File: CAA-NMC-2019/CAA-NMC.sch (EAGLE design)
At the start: 41 parts, among them IC1 ATTINY85-20SU, J1 M20-9980346

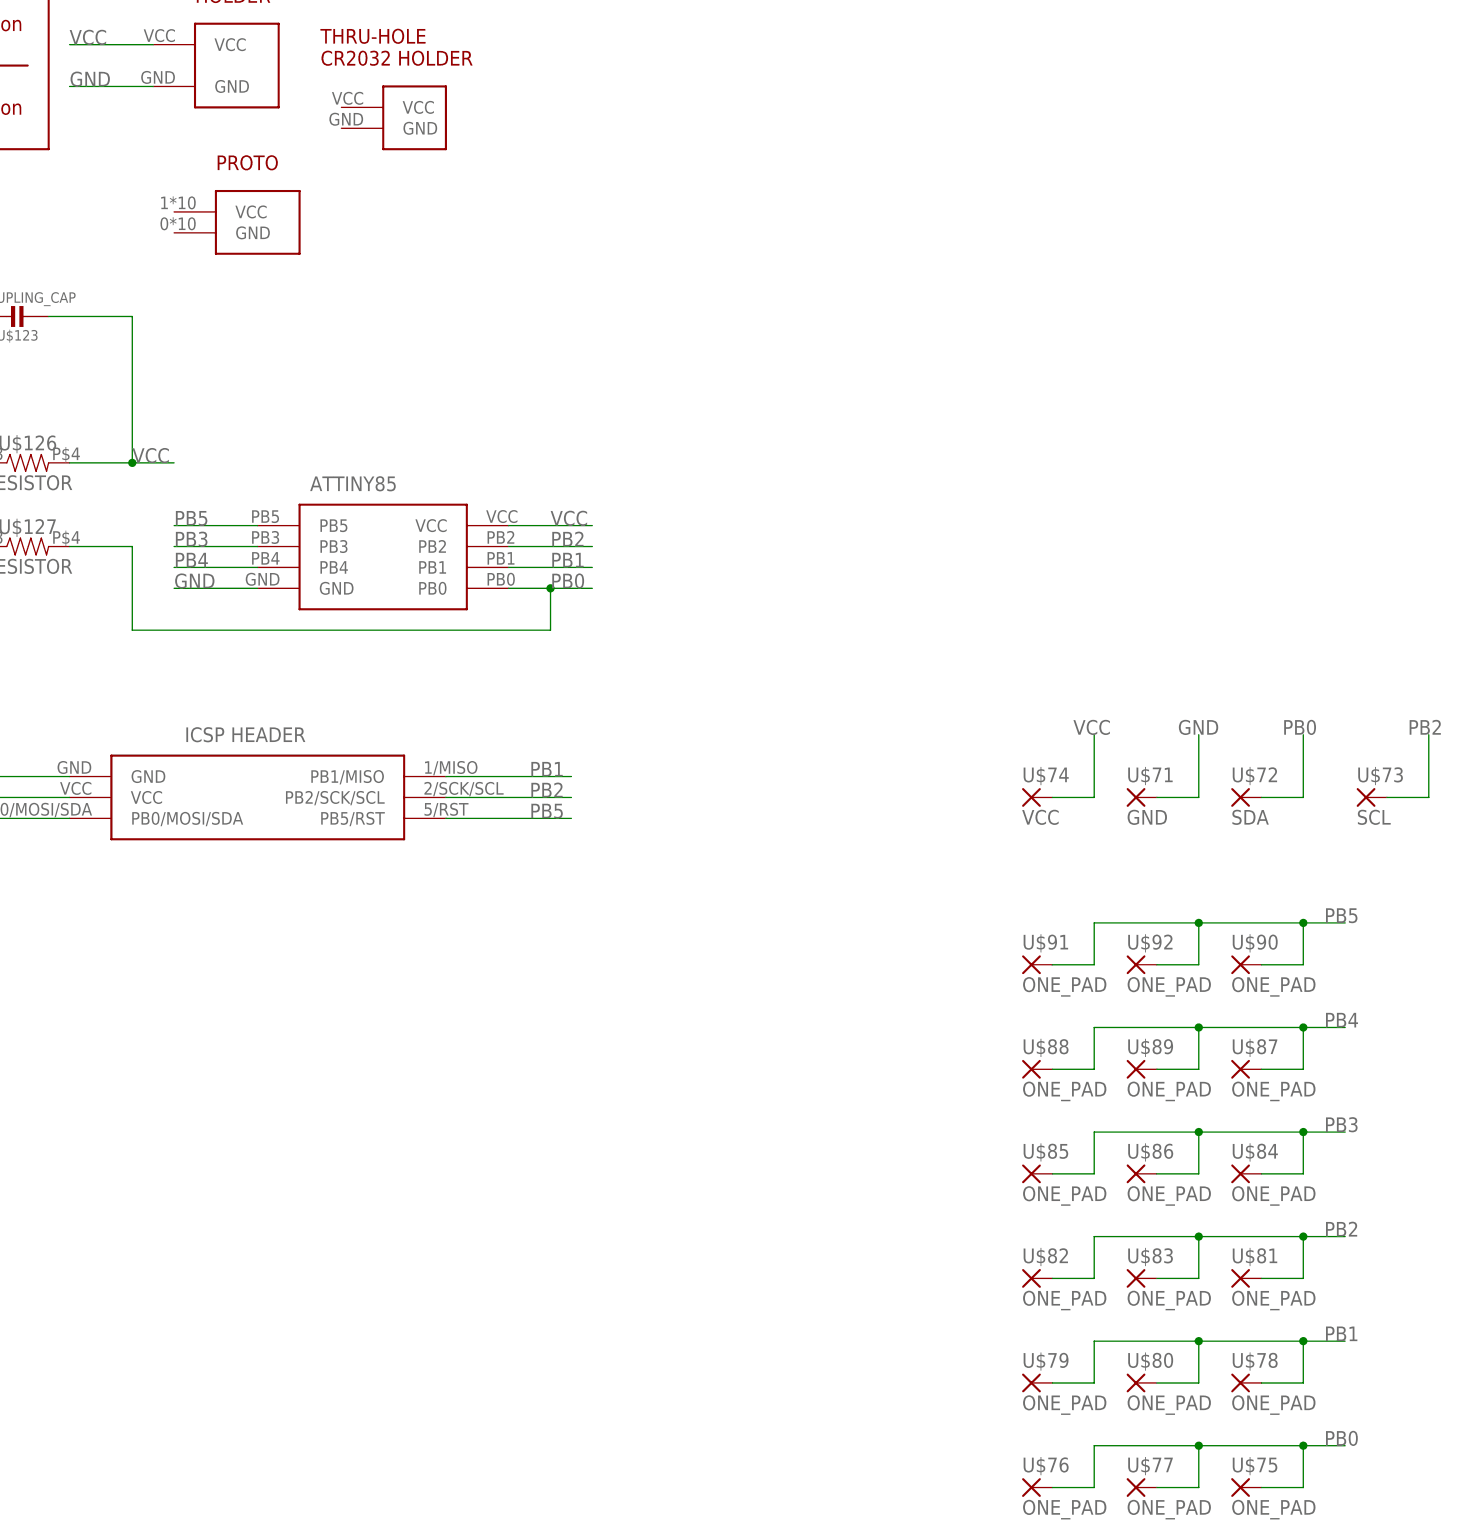
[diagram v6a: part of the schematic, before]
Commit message: added PB B/Os to proto grid
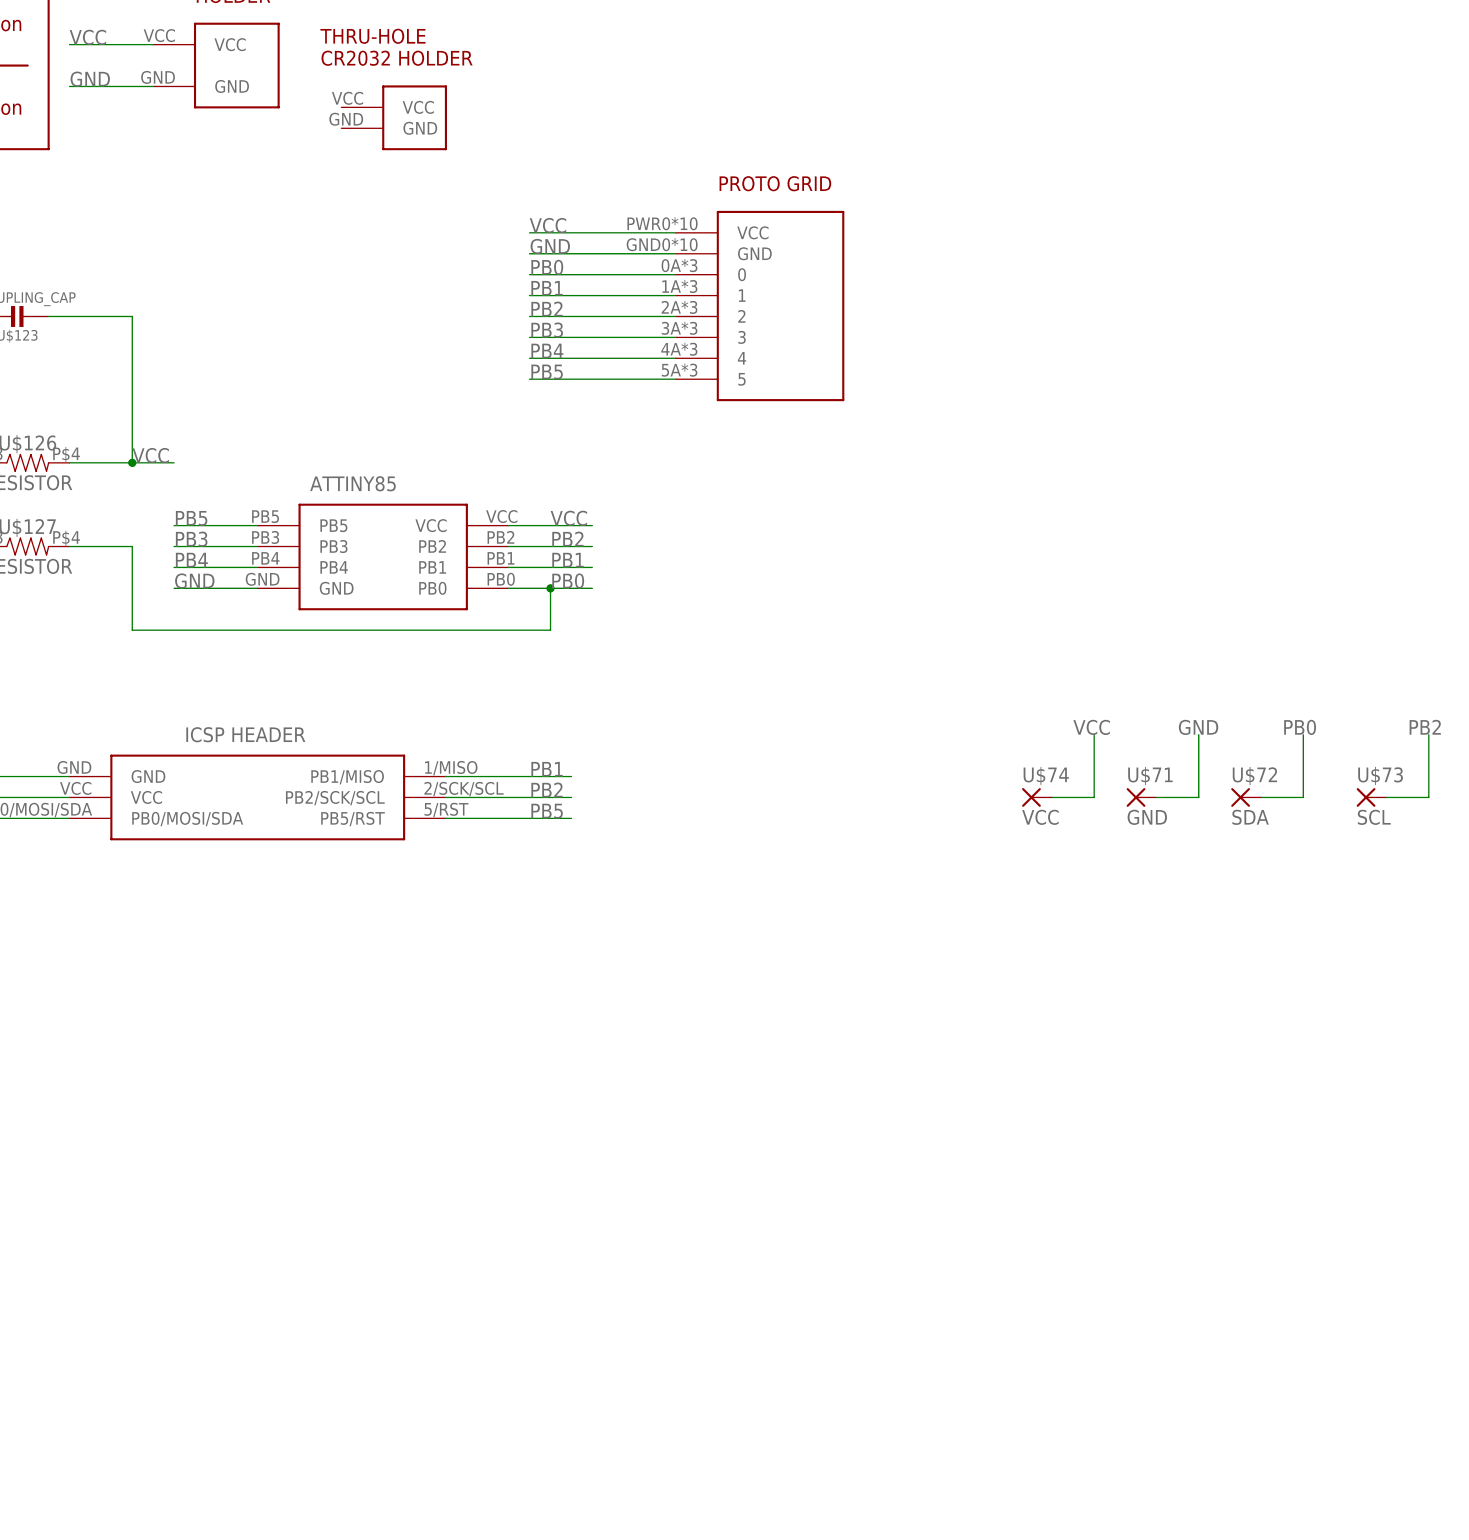
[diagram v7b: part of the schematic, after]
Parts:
- removed U$75, U$76, U$77, U$78, U$79, U$80, U$81, U$82, U$83, U$84, U$85, U$86, U$87, U$88, U$89, U$90, U$91, U$92: ONE_PAD, BadgeParts:ONE_PAD
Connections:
- net GND: now also U$1.GND
- net PB0: now also U$1.0; no longer U$75.P, U$76.P, U$77.P
- net PB1: now also U$1.1; no longer U$78.P, U$79.P, U$80.P
- net PB2: now also U$1.2; no longer U$81.P, U$82.P, U$83.P
- net PB3: now also U$1.3; no longer U$84.P, U$85.P, U$86.P
- net PB4: now also U$1.4; no longer U$87.P, U$88.P, U$89.P
- net PB5: now also U$1.5; no longer U$90.P, U$91.P, U$92.P
- net VCC: now also U$1.VCC

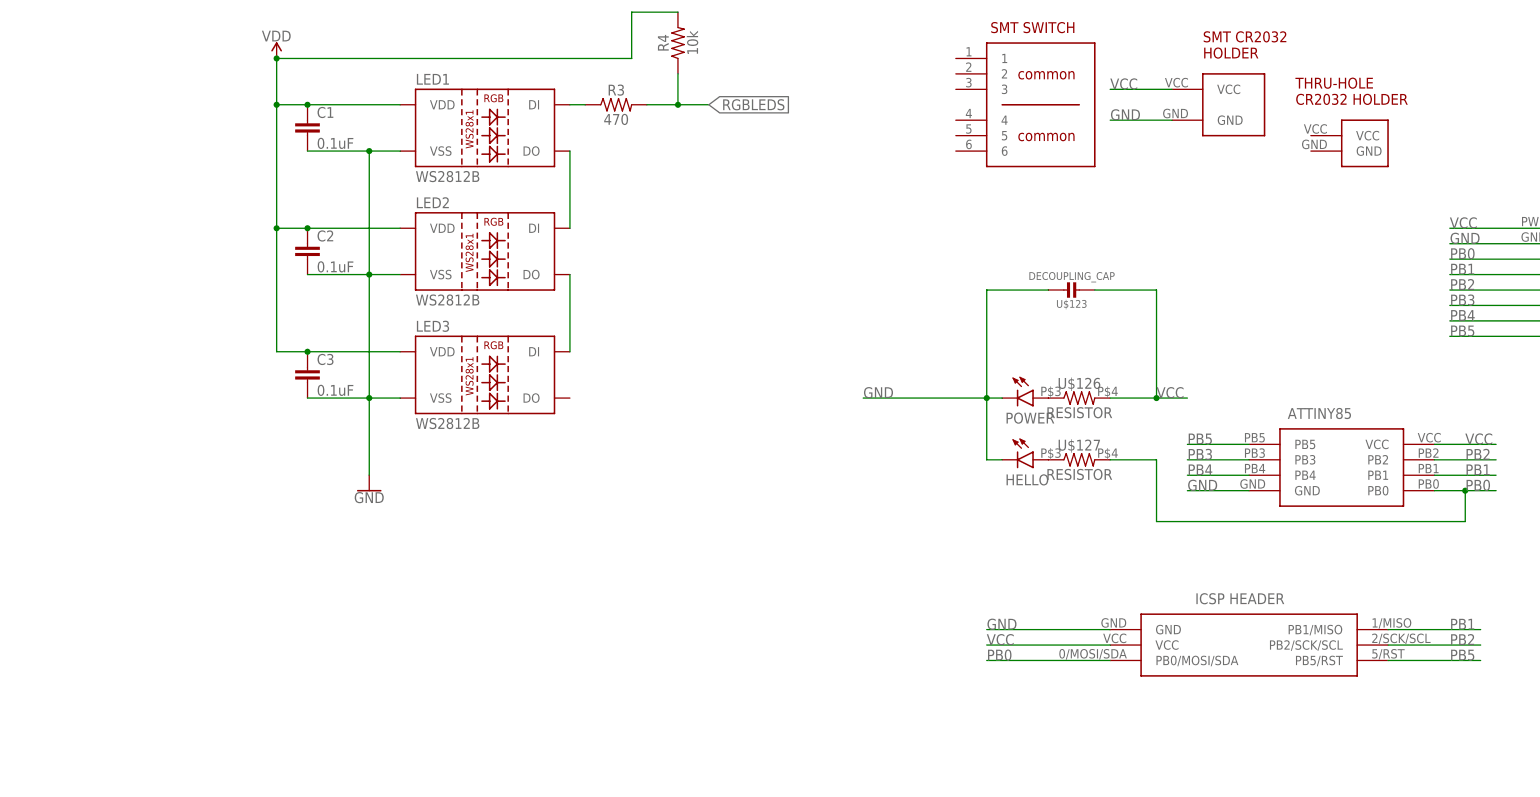
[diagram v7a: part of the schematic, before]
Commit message: custom RGB LED def includes .1uf cap in layout
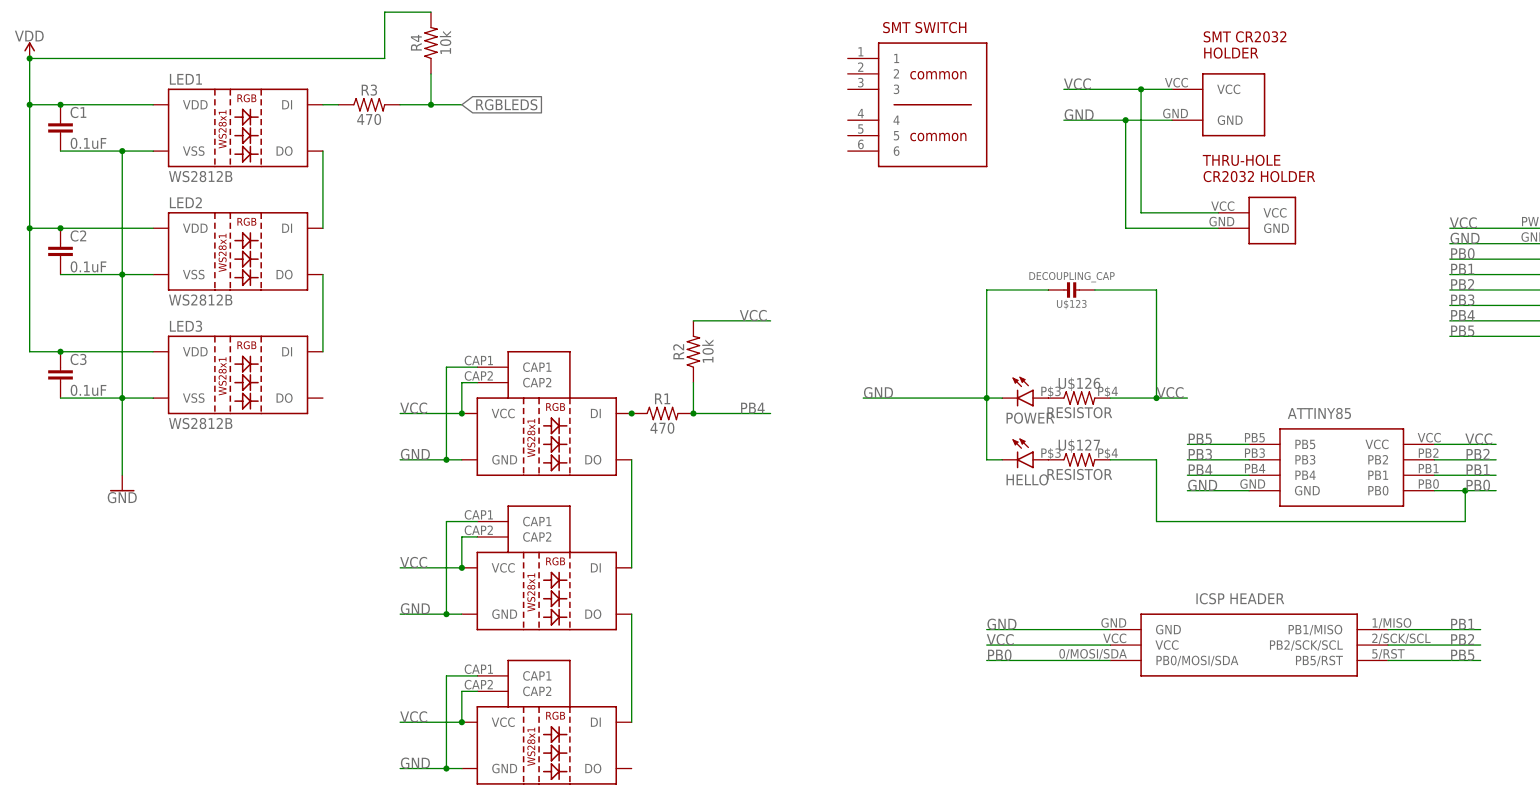
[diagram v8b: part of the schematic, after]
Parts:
- added D1, D2, D3: WS2812B, BadgeParts:WS2812B
- added R1: 470, SparkFun-Resistors:470OHM-0603-1/10W-1%
- added R2: 10k, SparkFun-Resistors:10KOHM-0603-1/10W-1%
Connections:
- new net N$3: D1.DO, D2.DI
- new net N$4: D2.DO, D3.DI
- new net N$5: D1.DI, R1.1
- net GND: now also D1.CAP1, D1.GND, D2.CAP1, D2.GND, D3.CAP1, D3.GND, U$2.GND
- net PB4: now also R1.2, R2.1
- net VCC: now also D1.CAP2, D1.VCC, D2.CAP2, D2.VCC, D3.CAP2, D3.VCC, R2.2, U$2.VCC
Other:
- moved on the sheet: C1, C2, C3, LED1, LED2, LED3, R3, R4
